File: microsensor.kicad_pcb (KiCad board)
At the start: 2 copper layers, 27 x 26 mm, 15 parts, among them J1 ARM SWD, SW1 Control, U1 BMD-360-A-R, U2 RV-3028-C7, U3 HDC2080

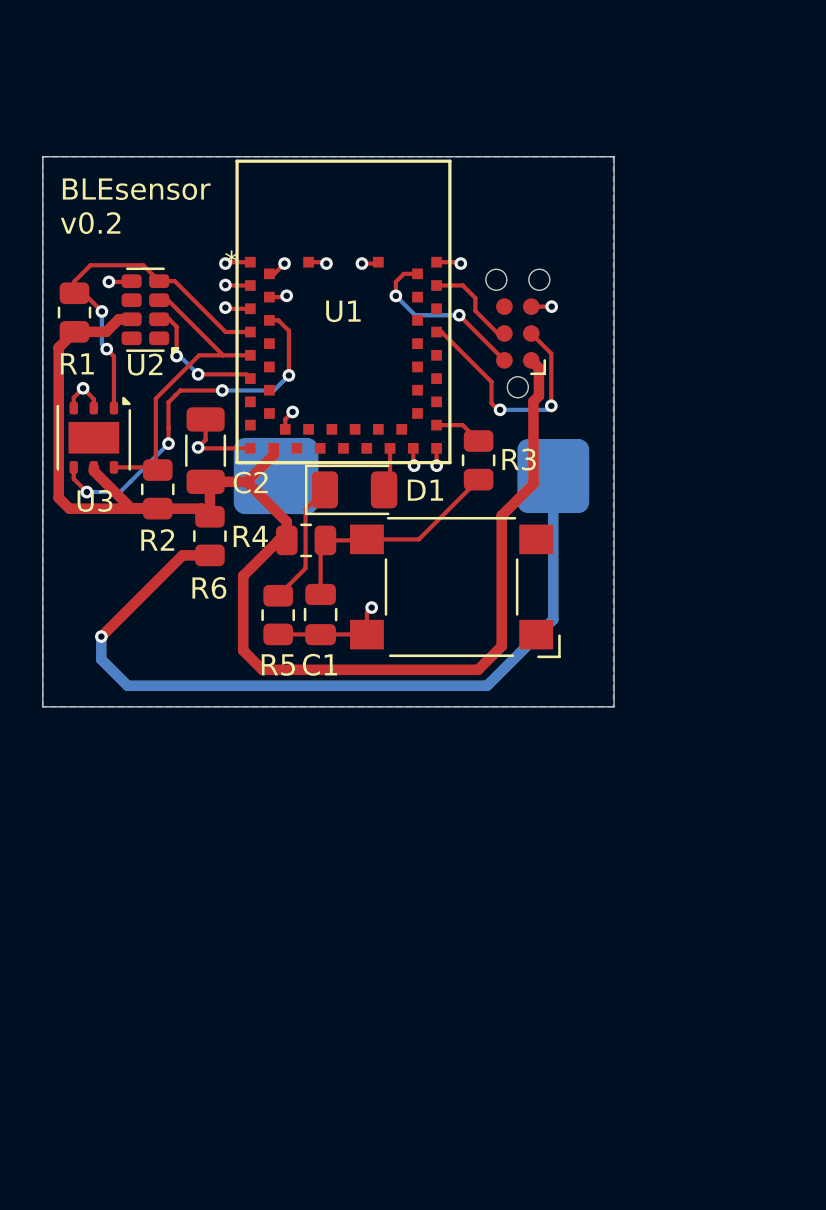
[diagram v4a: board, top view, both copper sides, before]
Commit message: Switch to nRF54L15 (NORA B206)
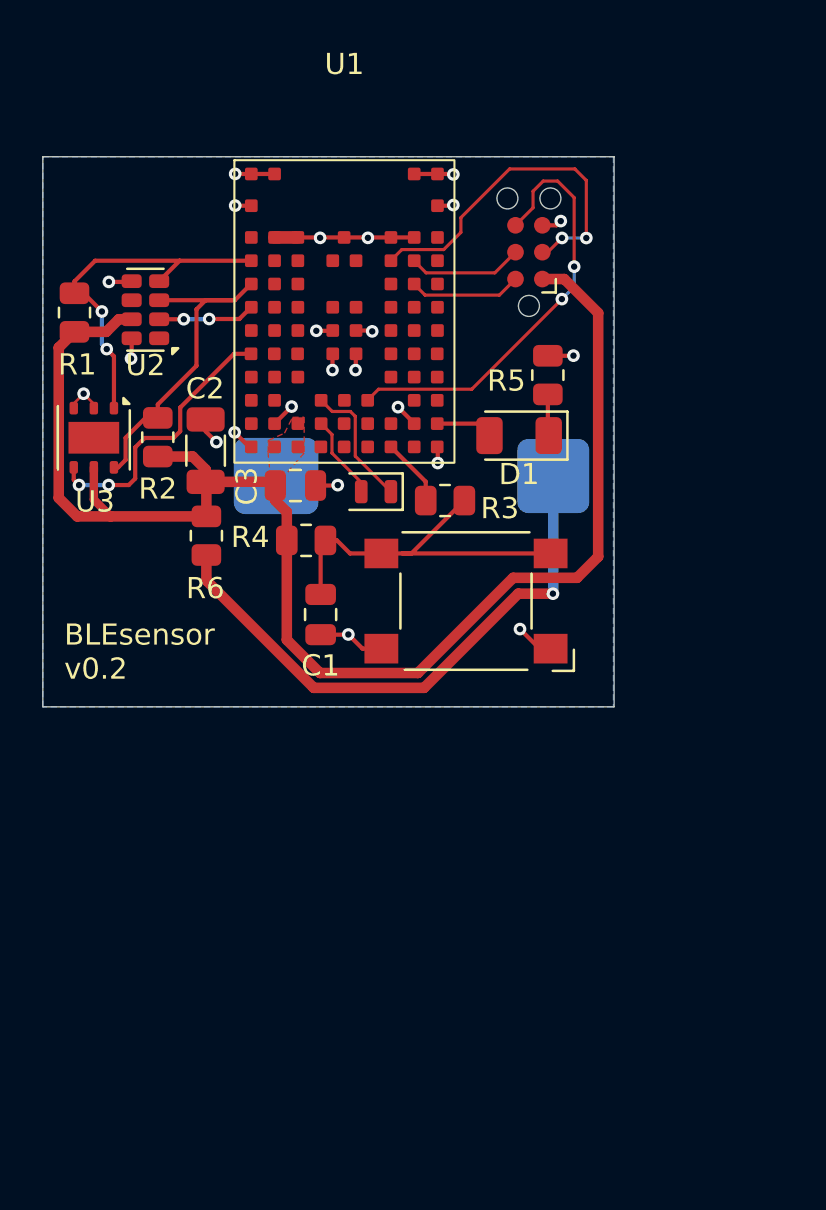
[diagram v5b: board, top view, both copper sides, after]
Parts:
- added C3: 100n, Capacitor_SMD:C_0805_2012Metric, F.Cu at (41.9, 45.5)
- added Y1: 32768, Crystal:Crystal_SMD_2012-2Pin_2.0x1.2mm, F.Cu at (45.8, 45.8)
- R5: value 330 -> 100
- U1: value BMD-360-A-R -> NORA B206; footprint footprints:BMD-360_UBL -> footprints:NORA-B2x6
- moved R5 17.1 mm to (53.9, 40.3), turned to 90 degrees
- moved D1 8.19 mm to (52.5, 43.2), turned to 180 degrees
- moved J1 3.88 mm to (53.0, 34.5)
- moved R3 2.48 mm to (49.0, 46.2), turned to 180 degrees
- moved R2 2.46 mm to (35.4, 43.3)
- moved SW1 0.95 mm to (50.0, 51.0)
- moved U1 0.88 mm to (44.3, 38.2)
- moved R6 0.17 mm to (37.7, 47.9)
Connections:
- D1 pad 2: Net-(D1-A) -> /LED
- J1 pad 2: SWDIO -> /SWDIO
- J1 pad 3: ~{RESET} -> /~{RESET}
- J1 pad 4: SWDCLK -> /SWDCLK
- J1 pad 6: unconnected-(J1-SWO-Pad6) -> /SWO
- R1 pad 2: SDA -> /SDA
- R2 pad 2: SCL -> /SCL
- R3 pad 2: /SWPUSH -> /~{SWPUSH}
- U2 pad 2: RTCINT -> /~{RTCINT}
- U2 pad 3: SCL -> /SCL
- U2 pad 4: SDA -> /SDA
- U2 pad 8: unconnected-(U2-EVI-Pad8) -> GND
- U3 pad 1: SDA -> /SDA
- U3 pad 4: TEMP_DRDY -> /T_DRDY
- U3 pad 6: SCL -> /SCL
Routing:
- net /SWO: track 0.00 -> 20.6 mm, vias 0 -> 2
- net TEMP_DRDY: track 17.6 -> 0.00 mm, vias 4 -> 0
- net SDA: track 17.0 -> 0.00 mm, vias 2 -> 0
- net /~{RESET}: track 0.00 -> 16.8 mm, vias 0 -> 2
- net /SDA: track 0.00 -> 16.7 mm, vias 0 -> 2
- net /SCL: track 0.00 -> 15.6 mm
- net SCL: track 15.0 -> 0.00 mm
- net /T_DRDY: track 0.00 -> 13.2 mm, vias 0 -> 2
- net ~{RESET}: track 11.4 -> 0.00 mm, vias 2 -> 0
- net /+BAT: track 37.8 -> 27.1 mm
- net SWDIO: track 8.24 -> 0.00 mm, vias 2 -> 0
- net GND: track 24.6 -> 31.2 mm, vias 16 -> 23
- net Net-(C1-Pad1): track 10.7 -> 17.2 mm
- net RTCINT: track 6.29 -> 0.00 mm, vias 2 -> 0
- net /XL2: track 0.00 -> 6.18 mm
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- added copper zone on F.Cu, net +3V3

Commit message: Finalize routing for NORA module Add and route VSENSE circuit
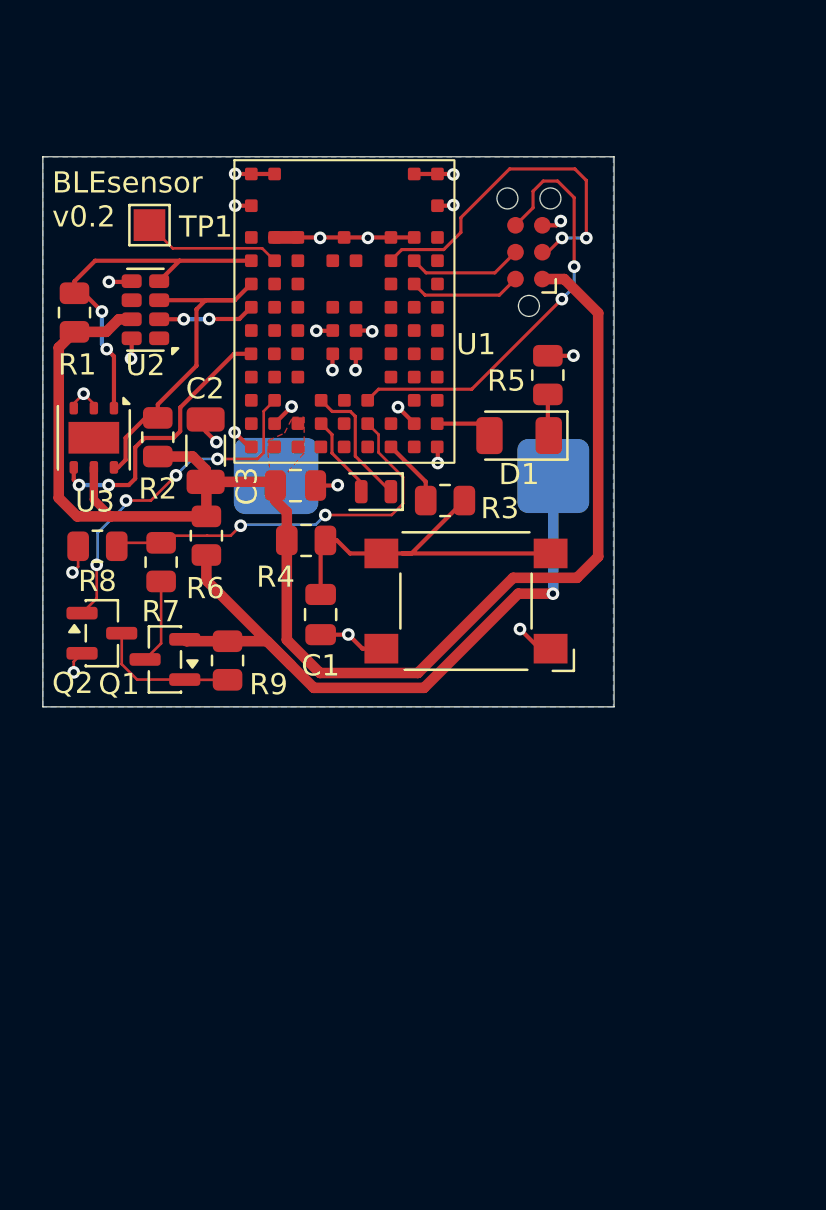
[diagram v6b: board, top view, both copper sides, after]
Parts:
- added Q1: TP0610T, Package_TO_SOT_SMD:SOT-23, F.Cu at (35.8, 53.8)
- added Q2: 2N7002, Package_TO_SOT_SMD:SOT-23, F.Cu at (32.8, 52.5)
- added R7: 330K, Resistor_SMD:R_0805_2012Metric, F.Cu at (35.6, 49.2)
- added R8: 220K, Resistor_SMD:R_0805_2012Metric, F.Cu at (32.6, 48.4)
- added R9: 100K, Resistor_SMD:R_0805_2012Metric, F.Cu at (38.7, 53.8)
- added TP1: P1.13, TestPoint:TestPoint_Pad_1.5x1.5mm, F.Cu at (35.0, 33.2)
- R5: value 100 -> 4.7K
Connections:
- net /+BAT renamed +BATT
- U1 pad B4: unconnected-(U1C-P1.12-PadB4) -> /VSENSE
- U1 pad C8: unconnected-(U1C-P0.02-PadC8) -> /VSENSE EN
- U1 pad J8: unconnected-(U1C-P1.13-PadJ8) -> Net-(TP1-Pad1)
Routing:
- net /VSENSE: track 0.00 -> 19.4 mm, vias 0 -> 2
- net /VSENSE EN: track 0.00 -> 16.3 mm, vias 0 -> 4
- net Net-(Q1-G): track 0.00 -> 6.77 mm
- net Net-(TP1-Pad1): track 0.00 -> 6.61 mm
- net +BATT: track 27.1 -> 32.6 mm
- net Net-(Q1-D): track 0.00 -> 4.00 mm
- net GND: track 31.2 -> 33.6 mm, vias 23 -> 25

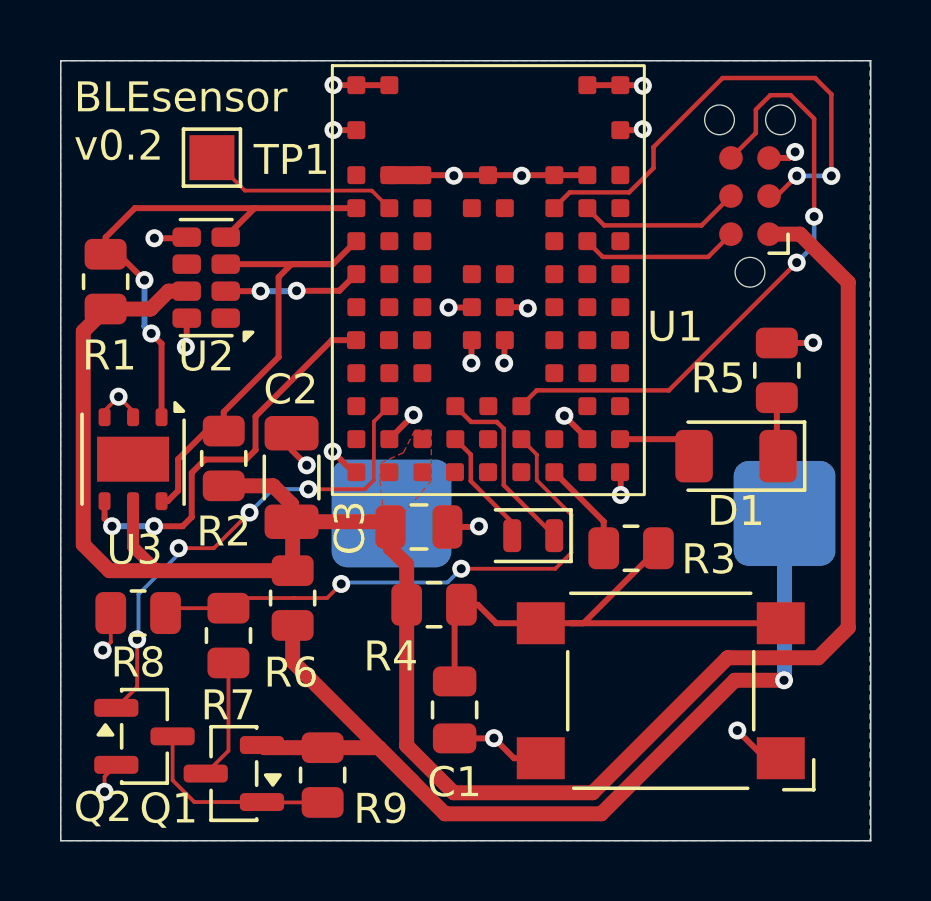
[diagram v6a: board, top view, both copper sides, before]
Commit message: Fix I2C routed to invalid pins Remove unnecessary N-MOS Adjust placement and routing Adjust annotations (order topologically)
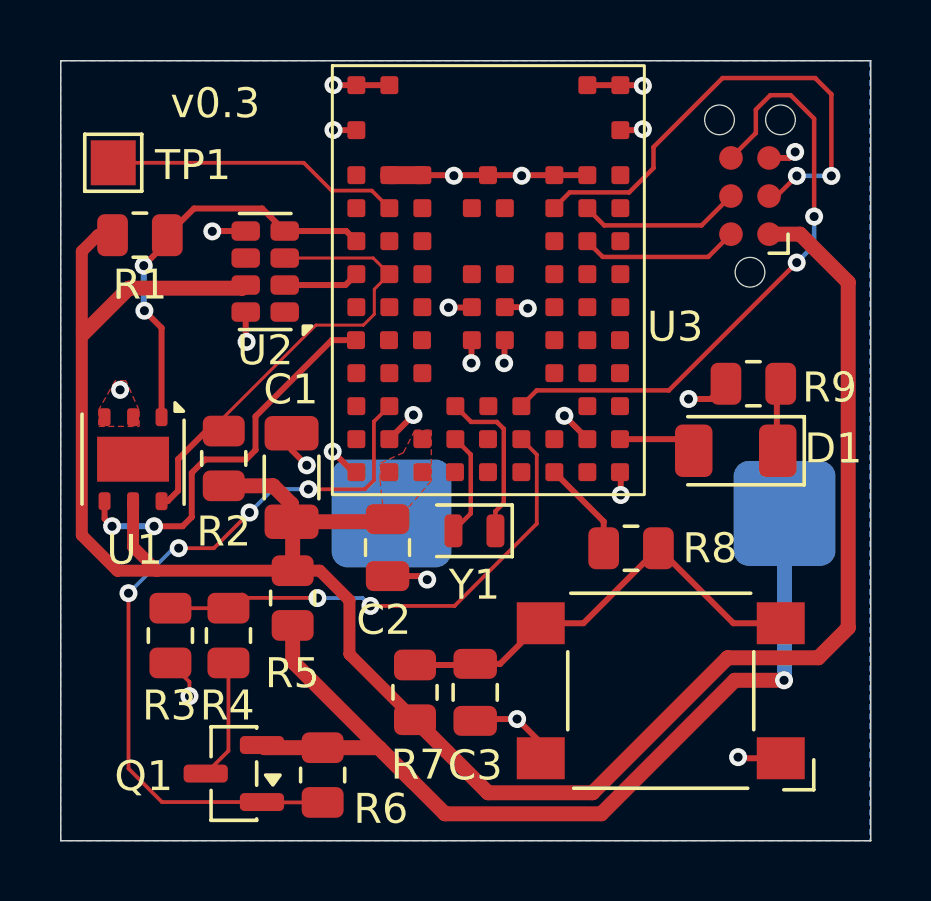
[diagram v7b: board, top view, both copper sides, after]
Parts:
- removed Q2: 2N7002, Package_TO_SOT_SMD:SOT-23
- Q1: value TP0610T -> IRLML2244TRPBF
- R3: renamed from R8; value 220K -> 100K
- moved TP1 3.29 mm to (31.8, 33.4)
- moved R7 2.99 mm to (41.8, 51.1), turned to -90 degrees
- moved U2 1.98 mm to (36.8, 37.0)
- moved Y1 1.97 mm to (43.8, 45.7)
- moved R1 1.93 mm to (32.6, 35.8), turned to 0 degrees
- moved R3 1.31 mm to (33.7, 49.2), turned to -90 degrees
- moved C2 1.25 mm to (40.9, 46.2), turned to -90 degrees
- moved R9 0.90 mm to (53.1, 40.8), turned to 180 degrees
- moved C3 0.90 mm to (43.8, 51.1)
- moved D1 0.18 mm to (52.5, 43.0)
- renumbered BT1 to BT0, C2 to C1, C3 to C2, C1 to C3, R7 to R4, R6 to R5, R9 to R6, R4 to R7, R3 to R8, R5 to R9, U3 to U1, U1 to U3
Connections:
- Q1 pad 1: Net-(Q1-G) -> /VSENSE EN
- R6 pad 2: Net-(Q1-G) -> /VSENSE EN
- U3 pad G8: unconnected-(U1C-P1.04-PadG8) -> /SCL
- U3 pad H9: /SCL -> /SDA
- U3 pad J9: /SDA -> unconnected-(U3C-P0.03-PadJ9)
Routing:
- net /VSENSE EN: track 16.3 -> 25.2 mm
- net Net-(Q1-G): track 6.77 -> 0.00 mm
- net +3V3: track 69.2 -> 74.5 mm
- net Net-(TP1-Pad1): track 6.61 -> 9.83 mm
- net /SDA: track 16.7 -> 13.5 mm
- net /VSENSE: track 19.4 -> 16.8 mm
- net Net-(C3-Pad1): track 17.2 -> 14.8 mm
- net GND: track 33.6 -> 31.3 mm, vias 25 -> 24
- net /~{RTCINT}: track 4.58 -> 2.54 mm, vias 2 -> 0
- net /SCL: track 15.6 -> 14.8 mm
- net /XL2: track 6.18 -> 5.44 mm
- added copper zone on F.Cu, net GND
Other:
- board text added: "v0.3"
- board text removed: "BLEsensor v0.2"

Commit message: v0.4 Switched to 4 layers Minor re-routing Changed button to smaller model Added mounting holes Added some missing 3d models
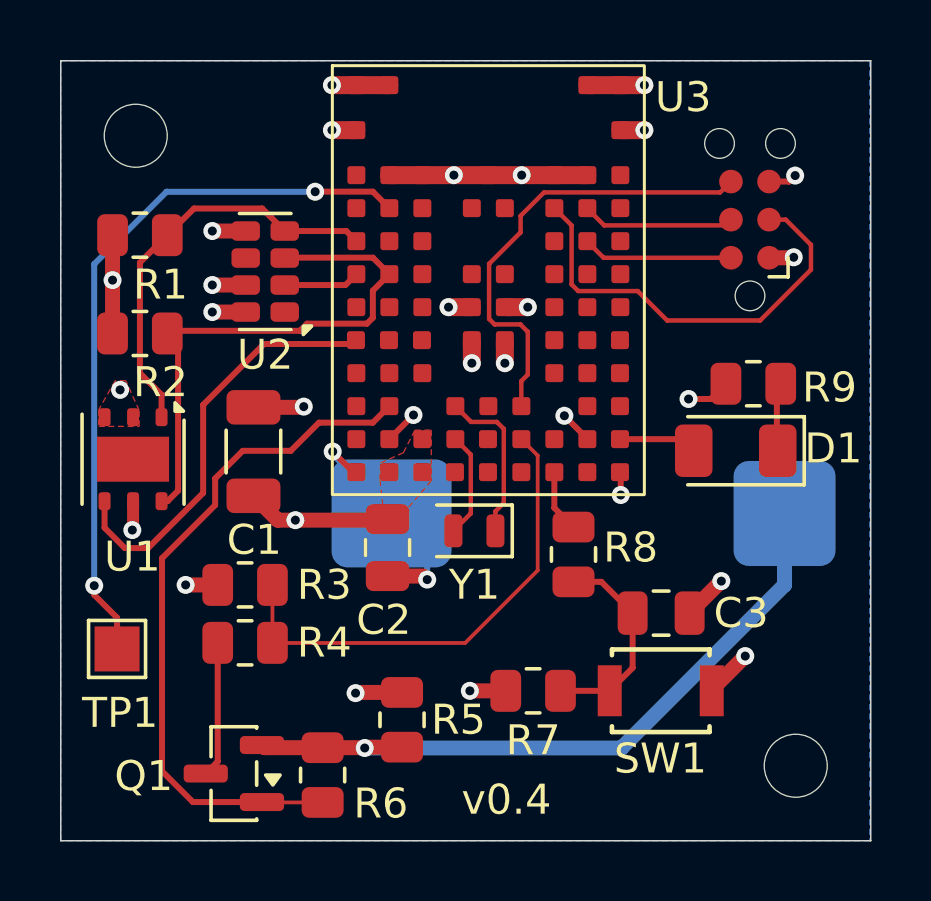
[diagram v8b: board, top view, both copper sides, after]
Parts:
- added MH1: MountingHole_2.1mm, MountingHole:MountingHole_2.1mm, F.Cu at (32.5, 32.5)
- added MH2: MountingHole_2.1mm, MountingHole:MountingHole_2.1mm, F.Cu at (54.5, 53.5)
- SW1: footprint Button_Switch_SMD:SW_SPST_Omron_B3FS-100xP -> footprints:B3U-1000P
- moved TP1 16.2 mm to (31.9, 49.6)
- moved C3 6.74 mm to (50.0, 48.4), turned to 0 degrees
- moved R5 5.46 mm to (41.4, 52.0)
- moved R2 5.02 mm to (32.6, 39.1), turned to 0 degrees
- moved R7 3.94 mm to (45.7, 51.0), turned to 180 degrees
- moved R3 3.01 mm to (36.1, 47.5), turned to 180 degrees
- moved R8 1.93 mm to (47.1, 46.5), turned to 90 degrees
- moved C1 1.54 mm to (36.4, 43.0)
- moved J1 0.79 mm to (53.0, 35.3)
- moved R4 0.61 mm to (36.1, 49.4), turned to 0 degrees
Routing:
- net +3V3: track 74.5 -> 13.7 mm, vias 0 -> 7
- net Net-(TP1-Pad1): track 9.83 -> 24.2 mm, vias 0 -> 2
- net +BATT: track 32.6 -> 23.3 mm
- net Net-(C3-Pad1): track 14.8 -> 6.95 mm
- net /SWO: track 20.6 -> 15.4 mm, vias 2 -> 0
- net GND: track 31.3 -> 34.7 mm
- net /SCL: track 14.8 -> 17.9 mm
- net /VSENSE EN: track 25.2 -> 23.1 mm, vias 4 -> 0
- net /~{RESET}: track 16.5 -> 14.5 mm, vias 2 -> 0
- net /~{SWPUSH}: track 3.22 -> 2.10 mm
- net /T_DRDY: track 13.2 -> 14.0 mm, vias 2 -> 0
- net /SWDCLK: track 5.44 -> 4.85 mm
- net Net-(Q1-D): track 4.00 -> 4.52 mm
- net /VSENSE: track 16.8 -> 16.4 mm, vias 2 -> 0
- net /SDA: track 13.5 -> 13.9 mm, vias 2 -> 0
- added copper zone on In2.Cu, net +3V3
- added copper zone on In1.Cu, net GND
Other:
- copper layers 2 -> 4
- board text added: "v0.4"
- board text removed: "v0.3"
